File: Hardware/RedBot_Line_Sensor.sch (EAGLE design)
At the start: 10 parts, among them U1 QRE1113SMD-W

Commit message: Updating 3 pin connector package
Updating 3 pin connector package to use new footprint that drops drill
hits for the connector's bosses down from 0.062' to 0.0535'. This will
help keep the part straight during reflow.
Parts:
- JP1: device SparkFun-Connectors:M03SMD_RA_MALE_POST -> SparkFun-Connectors:M031X03_SMD_RA_MALE_POST_SMALLER

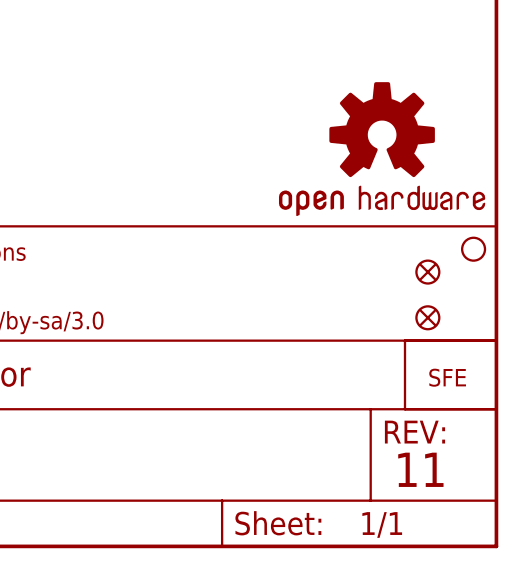
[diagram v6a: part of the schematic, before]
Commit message: removed micro fid. added regular
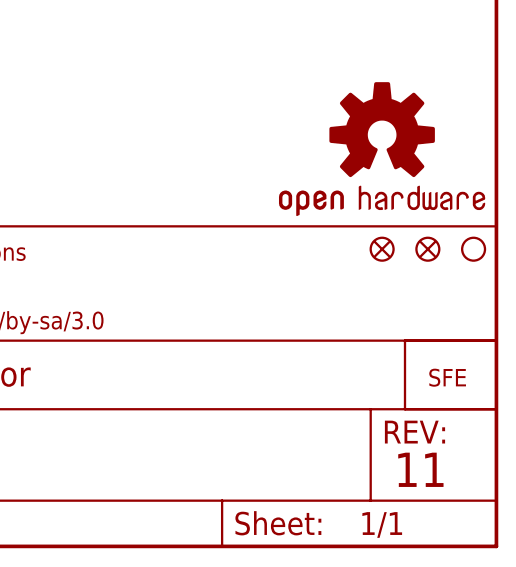
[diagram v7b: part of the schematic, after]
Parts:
- FID1, FID2: value FIDUCIALUFIDUCIAL -> FIDUCIAL1X2; device SparkFun-Aesthetics:FIDUCIALUFIDUCIAL -> SparkFun-Aesthetics:FIDUCIAL1X2
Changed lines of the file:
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@@
 <?xml version="1.0" encoding="utf-8"?>
 <!DOCTYPE eagle SYSTEM "eagle.dtd">
-<eagle version="6.5.0">
+<eagle version="6.6.0">
 <drawing>
 <settings>
@@
 <grid distance="0.1" unitdist="inch" unit="inch" style="lines" multiple="1" display="no" altdistance="0.01" altunitdist="inch" altunit="inch"/>
 <layers>
-<layer number="1" name="Top" color="4" fill="1" visible="yes" active="no"/>
-<layer number="2" name="Route2" color="1" fill="3" visible="yes" active="no"/>
-<layer number="3" name="Route3" color="4" fill="3" visible="yes" active="no"/>
-<layer number="4" name="Route4" color="1" fill="4" visible="yes" active="no"/>
-<layer number="5" name="Route5" color="4" fill="4" visible="yes" active="no"/>
-<layer number="6" name="Route6" color="1" fill="8" visible="yes" active="no"/>
-<layer number="7" name="Route7" color="4" fill="8" visible="yes" active="no"/>
-<layer number="8" name="Route8" color="1" fill="2" visible="yes" active="no"/>
-<layer number="9" name="Route9" color="4" fill="2" visible="yes" active="no"/>
-<layer number="10" name="Route10" color="1" fill="7" visible="yes" active="no"/>
-<layer number="11" name="Route11" color="4" fill="7" visible="yes" active="no"/>
-<layer number="12" name="Route12" color="1" fill="5" visible="yes" active="no"/>
-<layer number="13" name="Route13" color="4" fill="5" visible="yes" active="no"/>
-<layer number="14" name="Route14" color="1" fill="6" visible="yes" active="no"/>
-<layer number="15" name="Route15" color="4" fill="6" visible="yes" active="no"/>
-<layer number="16" name="Bottom" color="1" fill="1" visible="yes" active="no"/>
-<layer number="17" name="Pads" color="2" fill="1" visible="yes" active="no"/>
-<layer number="18" name="Vias" color="2" fill="1" visible="yes" active="no"/>
-<layer number="19" name="Unrouted" color="6" fill="1" visible="yes" active="no"/>
-<layer number="20" name="Dimension" color="15" fill="1" visible="yes" active="no"/>
-<layer number="21" name="tPlace" color="16" fill="1" visible="yes" active="no"/>
-<layer number="22" name="bPlace" color="14" fill="1" visible="yes" active="no"/>
-<layer number="23" name="tOrigins" color="15" fill="1" visible="yes" active="no"/>
-<layer number="24" name="bOrigins" color="15" fill="1" visible="yes" active="no"/>
-<layer number="25" name="tNames" color="7" fill="1" visible="yes" active="no"/>
-<layer number="26" name="bNames" color="7" fill="1" visible="yes" active="no"/>
-<layer number="27" name="tValues" color="7" fill="1" visible="yes" active="no"/>
-<layer number="28" name="bValues" color="7" fill="1" visible="yes" active="no"/>
+<layer number="1" name="Top" color="4" fill="1" visible="no" active="no"/>
+<layer number="2" name="Route2" color="1" fill="3" visible="no" active="no"/>
+<layer number="3" name="Route3" color="4" fill="3" visible="no" active="no"/>
+<layer number="4" name="Route4" color="1" fill="4" visible="no" active="no"/>
+<layer number="5" name="Route5" color="4" fill="4" visible="no" active="no"/>
+<layer number="6" name="Route6" color="1" fill="8" visible="no" active="no"/>
+<layer number="7" name="Route7" color="4" fill="8" visible="no" active="no"/>
+<layer number="8" name="Route8" color="1" fill="2" visible="no" active="no"/>
+<layer number="9" name="Route9" color="4" fill="2" visible="no" active="no"/>
+<layer number="10" name="Route10" color="1" fill="7" visible="no" active="no"/>
+<layer number="11" name="Route11" color="4" fill="7" visible="no" active="no"/>
+<layer number="12" name="Route12" color="1" fill="5" visible="no" active="no"/>
+<layer number="13" name="Route13" color="4" fill="5" visible="no" active="no"/>
+<layer number="14" name="Route14" color="1" fill="6" visible="no" active="no"/>
+<layer number="15" name="Route15" color="4" fill="6" visible="no" active="no"/>
+<layer number="16" name="Bottom" color="1" fill="1" visible="no" active="no"/>
+<layer number="17" name="Pads" color="2" fill="1" visible="no" active="no"/>
+<layer number="18" name="Vias" color="2" fill="1" visible="no" active="no"/>
+<layer number="19" name="Unrouted" color="6" fill="1" visible="no" active="no"/>
+<layer number="20" name="Dimension" color="15" fill="1" visible="no" active="no"/>
+<layer number="21" name="tPlace" color="16" fill="1" visible="no" active="no"/>
+<layer number="22" name="bPlace" color="14" fill="1" visible="no" active="no"/>
+<layer number="23" name="tOrigins" color="15" fill="1" visible="no" active="no"/>
+<layer number="24" name="bOrigins" color="15" fill="1" visible="no" active="no"/>
+<layer number="25" name="tNames" color="7" fill="1" visible="no" active="no"/>
+<layer number="26" name="bNames" color="7" fill="1" visible="no" active="no"/>
+<layer number="27" name="tValues" color="7" fill="1" visible="no" active="no"/>
+<layer number="28" name="bValues" color="7" fill="1" visible="no" active="no"/>
 <layer number="29" name="tStop" color="7" fill="3" visible="no" active="no"/>
 <layer number="30" name="bStop" color="7" fill="6" visible="no" active="no"/>
@@
 <layer number="35" name="tGlue" color="7" fill="4" visible="no" active="no"/>
 <layer number="36" name="bGlue" color="7" fill="5" visible="no" active="no"/>
-<layer number="37" name="tTest" color="7" fill="1" visible="yes" active="no"/>
-<layer number="38" name="bTest" color="7" fill="1" visible="yes" active="no"/>
+<layer number="37" name="tTest" color="7" fill="1" visible="no" active="no"/>
+<layer number="38" name="bTest" color="7" fill="1" visible="no" active="no"/>
 <layer number="39" name="tKeepout" color="4" fill="11" visible="no" active="no"/>
 <layer number="40" name="bKeepout" color="1" fill="11" visible="no" active="no"/>
@@
 <layer number="44" name="Drills" color="7" fill="1" visible="no" active="no"/>
 <layer number="45" name="Holes" color="7" fill="1" visible="no" active="no"/>
-<layer number="46" name="Milling" color="3" fill="1" visible="yes" active="no"/>
-<layer number="47" name="Measures" color="7" fill="1" visible="yes" active="no"/>
-<layer number="48" name="Document" color="7" fill="1" visible="yes" active="no"/>
-<layer number="49" name="Reference" color="7" fill="1" visible="yes" active="no"/>
-<layer number="50" name="dxf" color="7" fill="1" visible="yes" active="no"/>
-<layer number="51" name="tDocu" color="6" fill="1" visible="yes" active="no"/>
-<layer number="52" name="bDocu" color="7" fill="1" visible="yes" active="no"/>
-<layer number="53" name="tGND_GNDA" color="7" fill="9" visible="yes" active="no"/>
-<layer number="54" name="bGND_GNDA" color="1" fill="9" visible="yes" active="no"/>
-<layer number="56" name="wert" color="7" fill="1" visible="yes" active="no"/>
+<layer number="46" name="Milling" color="3" fill="1" visible="no" active="no"/>
+<layer number="47" name="Measures" color="7" fill="1" visible="no" active="no"/>
+<layer number="48" name="Document" color="7" fill="1" visible="no" active="no"/>
+<layer number="49" name="Reference" color="7" fill="1" visible="no" active="no"/>
+<layer number="50" name="dxf" color="7" fill="1" visible="no" active="no"/>
+<layer number="51" name="tDocu" color="6" fill="1" visible="no" active="no"/>
+<layer number="52" name="bDocu" color="7" fill="1" visible="no" active="no"/>
+<layer number="53" name="tGND_GNDA" color="7" fill="9" visible="no" active="no"/>
+<layer number="54" name="bGND_GNDA" color="1" fill="9" visible="no" active="no"/>
+<layer number="56" name="wert" color="7" fill="1" visible="no" active="no"/>
 <layer number="57" name="tCAD" color="7" fill="1" visible="no" active="no"/>
 <layer number="91" name="Nets" color="2" fill="1" visible="yes" active="yes"/>
@@
 <part name="STANDOFF1" library="SparkFun-Electromechanical" deviceset="STAND-OFF" device=""/>
 <part name="LOGO3" library="SparkFun-Aesthetics" deviceset="LOGO-SFE" device="SK"/>
-<part name="FID1" library="SparkFun-Aesthetics" deviceset="FIDUCIAL" device="UFIDUCIAL"/>
-<part name="FID2" library="SparkFun-Aesthetics" deviceset="FIDUCIAL" device="UFIDUCIAL"/>
+<part name="FID1" library="SparkFun-Aesthetics" deviceset="FIDUCIAL" device="1X2"/>
+<part name="FID2" library="SparkFun-Aesthetics" deviceset="FIDUCIAL" device="1X2"/>
 </parts>
 <sheets>
@@
 <instance part="STANDOFF1" gate="G$1" x="246.38" y="33.02"/>
 <instance part="LOGO3" gate="G$1" x="241.3" y="17.78"/>
-<instance part="FID1" gate="G$1" x="241.3" y="30.48"/>
-<instance part="FID2" gate="G$1" x="241.3" y="25.4"/>
+<instance part="FID1" gate="G$1" x="241.3" y="33.02"/>
+<instance part="FID2" gate="G$1" x="236.22" y="33.02"/>
 </instances>
 <busses>
